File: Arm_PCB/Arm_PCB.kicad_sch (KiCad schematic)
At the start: 30 parts, among them J1 Conn_02x04_Counter_Clockwise, J10 Conn_02x02_Counter_Clockwise, J11 Conn_02x04_Counter_Clockwise, J12 Screw_Terminal_01x02, J13 Screw_Terminal_01x02, J14 Screw_Terminal_01x02, J15 Screw_Terminal_01x02, J16 Screw_Terminal_01x02, J17 Screw_Terminal_01x02, J18 Screw_Terminal_01x02, J2 Conn_02x04_Counter_Clockwise, J3 Conn_02x04_Counter_Clockwise, J4 Conn_02x04_Counter_Clockwise, J5 Conn_02x03_Counter_Clockwise, J7 Conn_02x03_Counter_Clockwise, J8 Conn_02x02_Counter_Clockwise, J9 Conn_02x04_Counter_Clockwise, SW1 SW_Push, SW2 SW_Push, SW3 SW_Push, SW4 SW_Push

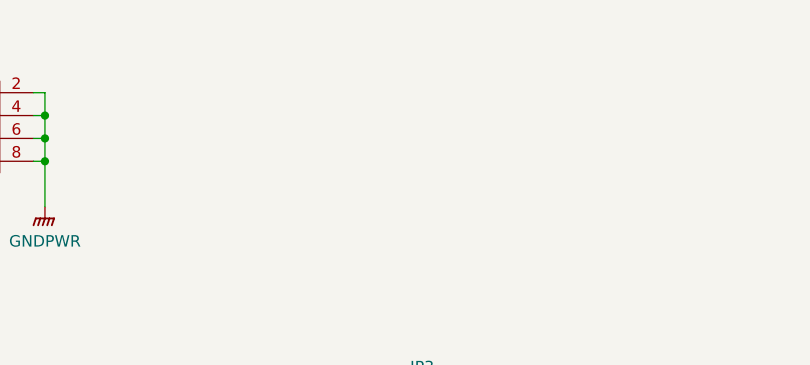
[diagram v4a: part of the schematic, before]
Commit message: Add mounting holes, other minor changes
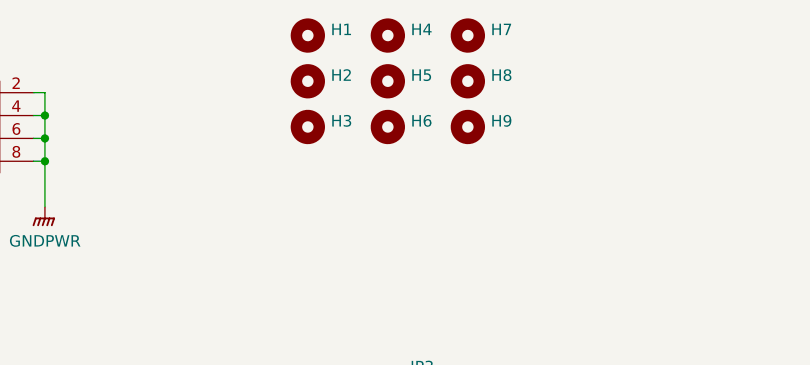
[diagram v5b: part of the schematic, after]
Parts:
- added H1, H2, H3, H4, H5, H6, H7, H8, H9: MountingHole, MountingHole:MountingHole_4.3mm_M4, symbol Mechanical:MountingHole
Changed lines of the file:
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@@
+    )
+  )
+  (symbol (lib_id "Mechanical:MountingHole") (at 100.33 22.86 0) (unit 1)
+    (in_bom yes) (on_board yes) (dnp no) (fields_autoplaced)
+    (property "Reference" "H5" (at 102.87 22.225 0)
+      (effects (font (size 1.27 1.27)) (justify left))
+    )
+    (property "Value" "MountingHole" (at 102.87 24.765 0)
+      (effects (font (size 1.27 1.27)) (justify left) hide)
+    )
+    (property "Footprint" "MountingHole:MountingHole_4.3mm_M4" (at 100.33 22.86 0)
+      (effects (font (size 1.27 1.27)) hide)
+    )
+    (property "Datasheet" "~" (at 100.33 22.86 0)
+      (effects (font (size 1.27 1.27)) hide)
+    )
+    (instances
+      (project "Arm_PCB"
+        (path "/f8b9fbb1-757f-4aa8-8e30-7f83a30c7c5f"
+          (reference "H5") (unit 1)
+        )
+      )
     )
   )
@@
     )
   )
+  (symbol (lib_id "Mechanical:MountingHole") (at 109.22 17.78 0) (unit 1)
+    (in_bom yes) (on_board yes) (dnp no) (fields_autoplaced)
+    (property "Reference" "H7" (at 111.76 17.145 0)
+      (effects (font (size 1.27 1.27)) (justify left))
+    )
+    (property "Value" "MountingHole" (at 111.76 19.685 0)
+      (effects (font (size 1.27 1.27)) (justify left) hide)
+    )
+    (property "Footprint" "MountingHole:MountingHole_4.3mm_M4" (at 109.22 17.78 0)
+      (effects (font (size 1.27 1.27)) hide)
+    )
+    (property "Datasheet" "~" (at 109.22 17.78 0)
+      (effects (font (size 1.27 1.27)) hide)
+    )
+    (instances
+      (project "Arm_PCB"
+        (path "/f8b9fbb1-757f-4aa8-8e30-7f83a30c7c5f"
+          (reference "H7") (unit 1)
+        )
+      )
+    )
+  )
   (symbol (lib_id "power:+3.3V") (at 240.03 139.7 0) (unit 1)
     (in_bom yes) (on_board yes) (dnp no)
@@
     )
   )
+  (symbol (lib_id "Mechanical:MountingHole") (at 109.22 27.94 0) (unit 1)
+    (in_bom yes) (on_board yes) (dnp no) (fields_autoplaced)
+    (property "Reference" "H9" (at 111.76 27.305 0)
+      (effects (font (size 1.27 1.27)) (justify left))
+    )
+    (property "Value" "MountingHole" (at 111.76 29.845 0)
+      (effects (font (size 1.27 1.27)) (justify left) hide)
+    )
+    (property "Footprint" "MountingHole:MountingHole_4.3mm_M4" (at 109.22 27.94 0)
+      (effects (font (size 1.27 1.27)) hide)
+    )
+    (property "Datasheet" "~" (at 109.22 27.94 0)
+      (effects (font (size 1.27 1.27)) hide)
+    )
+    (instances
+      (project "Arm_PCB"
+        (path "/f8b9fbb1-757f-4aa8-8e30-7f83a30c7c5f"
+          (reference "H9") (unit 1)
+        )
+      )
+    )
+  )
   (symbol (lib_id "Jumper:Jumper_2_Open") (at 15.24 162.56 270) (unit 1)
     (in_bom yes) (on_board yes) (dnp no) (fields_autoplaced)
@@
         (path "/f8b9fbb1-757f-4aa8-8e30-7f83a30c7c5f"
           (reference "SW3") (unit 1)
+        )
+      )
+    )
+  )
+  (symbol (lib_id "Mechanical:MountingHole") (at 100.33 27.94 0) (unit 1)
+    (in_bom yes) (on_board yes) (dnp no) (fields_autoplaced)
+    (property "Reference" "H6" (at 102.87 27.305 0)
+      (effects (font (size 1.27 1.27)) (justify left))
+    )
+    (property "Value" "MountingHole" (at 102.87 29.845 0)
+      (effects (font (size 1.27 1.27)) (justify left) hide)
+    )
+    (property "Footprint" "MountingHole:MountingHole_4.3mm_M4" (at 100.33 27.94 0)
+      (effects (font (size 1.27 1.27)) hide)
+    )
+    (property "Datasheet" "~" (at 100.33 27.94 0)
+      (effects (font (size 1.27 1.27)) hide)
+    )
+    (instances
+      (project "Arm_PCB"
+        (path "/f8b9fbb1-757f-4aa8-8e30-7f83a30c7c5f"
+          (reference "H6") (unit 1)
         )
       )
@@
     )
   )
+  (symbol (lib_id "Mechanical:MountingHole") (at 91.44 22.86 0) (unit 1)
+    (in_bom yes) (on_board yes) (dnp no) (fields_autoplaced)
+    (property "Reference" "H2" (at 93.98 22.225 0)
+      (effects (font (size 1.27 1.27)) (justify left))
+    )
+    (property "Value" "MountingHole" (at 93.98 24.765 0)
+      (effects (font (size 1.27 1.27)) (justify left) hide)
+    )
+    (property "Footprint" "MountingHole:MountingHole_4.3mm_M4" (at 91.44 22.86 0)
+      (effects (font (size 1.27 1.27)) hide)
+    )
+    (property "Datasheet" "~" (at 91.44 22.86 0)
+      (effects (font (size 1.27 1.27)) hide)
+    )
+    (instances
+      (project "Arm_PCB"
+        (path "/f8b9fbb1-757f-4aa8-8e30-7f83a30c7c5f"
+          (reference "H2") (unit 1)
+        )
+      )
+    )
+  )
   (symbol (lib_id "power:GND") (at 238.76 72.39 0) (unit 1)
     (in_bom yes) (on_board yes) (dnp no)
@@
     )
   )
+  (symbol (lib_id "Mechanical:MountingHole") (at 91.44 27.94 0) (unit 1)
+    (in_bom yes) (on_board yes) (dnp no) (fields_autoplaced)
+    (property "Reference" "H3" (at 93.98 27.305 0)
+      (effects (font (size 1.27 1.27)) (justify left))
+    )
+    (property "Value" "MountingHole" (at 93.98 29.845 0)
+      (effects (font (size 1.27 1.27)) (justify left) hide)
+    )
+    (property "Footprint" "MountingHole:MountingHole_4.3mm_M4" (at 91.44 27.94 0)
+      (effects (font (size 1.27 1.27)) hide)
+    )
+    (property "Datasheet" "~" (at 91.44 27.94 0)
+      (effects (font (size 1.27 1.27)) hide)
+    )
+    (instances
+      (project "Arm_PCB"
+        (path "/f8b9fbb1-757f-4aa8-8e30-7f83a30c7c5f"
+          (reference "H3") (unit 1)
+        )
+      )
+    )
+  )
   (symbol (lib_name "GNDPWR_2") (lib_id "power:GNDPWR") (at 245.11 72.39 0) (unit 1)
     (in_bom yes) (on_board yes) (dnp no)
@@
         (path "/f8b9fbb1-757f-4aa8-8e30-7f83a30c7c5f"
           (reference "JP2") (unit 1)
+        )
+      )
+    )
+  )
+  (symbol (lib_id "Mechanical:MountingHole") (at 109.22 22.86 0) (unit 1)
+    (in_bom yes) (on_board yes) (dnp no) (fields_autoplaced)
+    (property "Reference" "H8" (at 111.76 22.225 0)
+      (effects (font (size 1.27 1.27)) (justify left))
+    )
+    (property "Value" "MountingHole" (at 111.76 24.765 0)
+      (effects (font (size 1.27 1.27)) (justify left) hide)
+    )
+    (property "Footprint" "MountingHole:MountingHole_4.3mm_M4" (at 109.22 22.86 0)
+      (effects (font (size 1.27 1.27)) hide)
+    )
+    (property "Datasheet" "~" (at 109.22 22.86 0)
+      (effects (font (size 1.27 1.27)) hide)
+    )
+    (instances
+      (project "Arm_PCB"
+        (path "/f8b9fbb1-757f-4aa8-8e30-7f83a30c7c5f"
+          (reference "H8") (unit 1)
         )
       )
@@
     )
   )
+  (symbol (lib_id "Mechanical:MountingHole") (at 91.44 17.78 0) (unit 1)
+    (in_bom yes) (on_board yes) (dnp no) (fields_autoplaced)
+    (property "Reference" "H1" (at 93.98 17.145 0)
+      (effects (font (size 1.27 1.27)) (justify left))
+    )
+    (property "Value" "MountingHole" (at 93.98 19.685 0)
+      (effects (font (size 1.27 1.27)) (justify left) hide)
+    )
+    (property "Footprint" "MountingHole:MountingHole_4.3mm_M4" (at 91.44 17.78 0)
+      (effects (font (size 1.27 1.27)) hide)
+    )
+    (property "Datasheet" "~" (at 91.44 17.78 0)
+      (effects (font (size 1.27 1.27)) hide)
+    )
+    (instances
+      (project "Arm_PCB"
+        (path "/f8b9fbb1-757f-4aa8-8e30-7f83a30c7c5f"
+          (reference "H1") (unit 1)
+        )
+      )
+    )
+  )
   (symbol (lib_name "+3.3V_1") (lib_id "power:+3.3V") (at 15.24 154.94 0) (unit 1)
     (in_bom yes) (on_board yes) (dnp no) (fields_autoplaced)
@@
         )
       )
+    )
+  )
+  (symbol (lib_id "Mechanical:MountingHole") (at 100.33 17.78 0) (unit 1)
+    (in_bom yes) (on_board yes) (dnp no) (fields_autoplaced)
+    (property "Reference" "H4" (at 102.87 17.145 0)
+      (effects (font (size 1.27 1.27)) (justify left))
+    )
+    (property "Value" "MountingHole" (at 102.87 19.685 0)
+      (effects (font (size 1.27 1.27)) (justify left) hide)
+    )
+    (property "Footprint" "MountingHole:MountingHole_4.3mm_M4" (at 100.33 17.78 0)
+      (effects (font (size 1.27 1.27)) hide)
+    )
+    (property "Datasheet" "~" (at 100.33 17.78 0)
+      (effects (font (size 1.27 1.27)) hide)
+    )
+    (instances
+      (project "Arm_PCB"
+        (path "/f8b9fbb1-757f-4aa8-8e30-7f83a30c7c5f"
+          (reference "H4") (unit 1)
+        )
+      )
